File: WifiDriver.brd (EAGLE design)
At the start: 107.6 x 50.8 mm, 8 parts, among them U1 ESP32-DEVKITC-32U, U2 ESP32-DEVKITC-32U, U3 DS18B20

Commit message: Adding files
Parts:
- removed JP2, JP4, JP5: (no value), pinhead:1X05
- added R2, R3, R4, R5: 0, adafruit:R0805
- added U$1: GPS_MOD, brandon_parts:GPS_NEO_6M
- moved R1 40.1 mm to (40.3, 8.59), turned to 90 degrees
- moved U3 28.3 mm to (63.0, 3.70)
- moved U2 21.7 mm to (21.6, 45.1)
- moved U1 20.6 mm to (51.9, 45.0)
- moved JP1 13.3 mm to (70.6, 55.2)
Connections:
- new net ESP_A_RX: R3.1, U1.11
- new net ESP_A_TX: R2.1, U1.12
- new net ESP_B_RX: R4.2, U2.11
- new net ESP_B_TX: R5.2, U2.12
- new net N$2: R3.2, R5.1
- new net N$3: U1.7, U2.15
- net 5V: now also R1.2, U$1.VCC; no longer JP2.5, JP4.3, JP5.3
- net DQ: now also R1.1, U1.26, U3.2; no longer R1.2
- net ESP32_1_RX: no longer JP4.4
- net ESP32_1_TX: no longer JP4.5
- net ESP32_2_RX: no longer JP5.4
- net ESP32_2_TX: no longer JP5.5
- net GND: now also U$1.GND; no longer JP2.4, JP4.1, JP5.1
- net GPS_RX: now also U$1.RXD; no longer JP2.2
- net GPS_TX: now also U$1.TXD; no longer JP2.3
- net N$1: now also R2.2, R4.1; no longer R1.1, U3.2
- net PPS: now also U$1.PPS; no longer JP2.1
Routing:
- net N$1: track 0.00 -> 2.79 mm
- net N$2: track 0.00 -> 2.68 mm
- net CLK: track 2.55 -> 0.00 mm
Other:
- board size 107.6 x 50.8 mm -> 99 x 70.8 mm

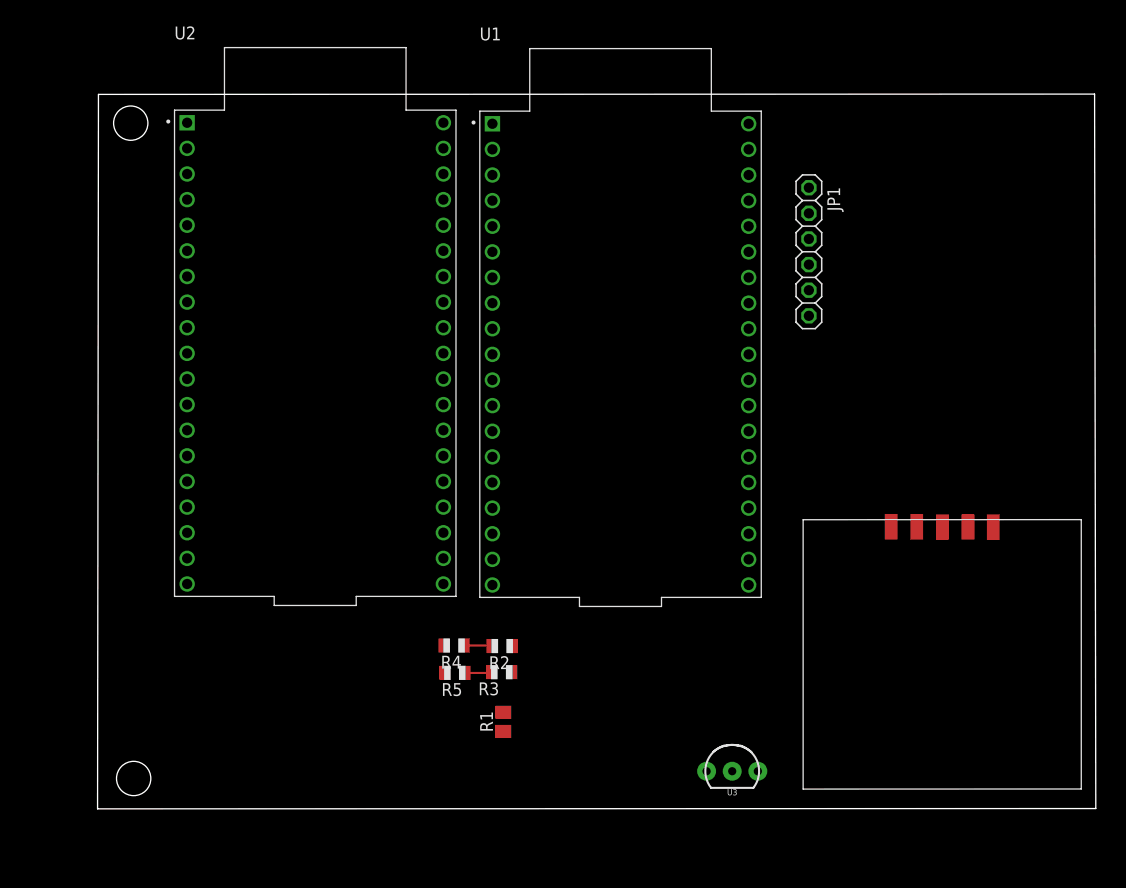
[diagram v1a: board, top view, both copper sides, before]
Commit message: Updated with wardriver_v3 pinout from original author
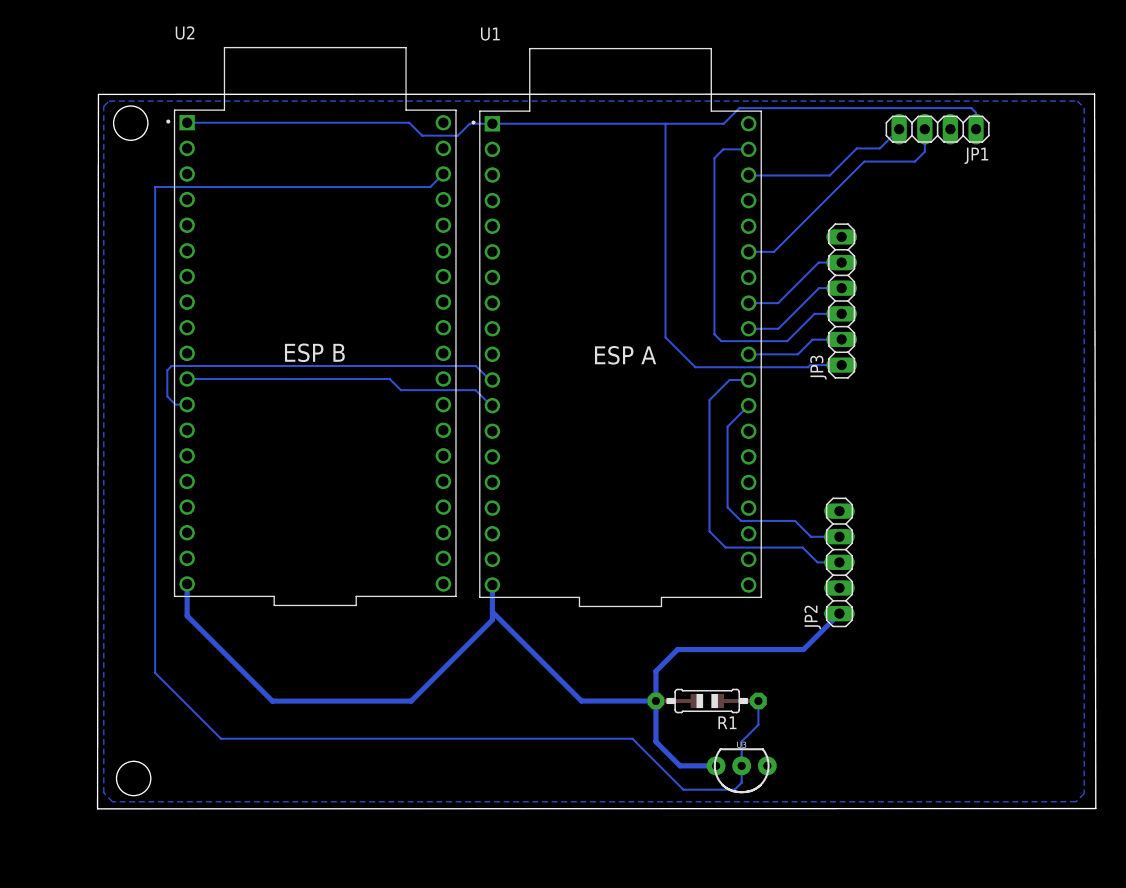
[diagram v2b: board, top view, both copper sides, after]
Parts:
- removed R2, R3, R4, R5: 0, adafruit:R0805
- removed U$1: GPS_MOD, brandon_parts:GPS_NEO_6M
- added JP2: (no value), pinhead:1X05
- added JP3: (no value), pinhead:1X06
- JP1: device adafruit:1X06 -> pinhead:1X04
- R1: value (none) -> 4.7k; device adafruit:M0805 -> adafruit:0805-THM
- moved R1 20.3 mm to (60.5, 10.7), turned to 180 degrees
- moved JP1 17.6 mm to (83.3, 67.3), turned to 180 degrees
- moved U3 1.08 mm to (63.9, 4.23), turned to 180 degrees
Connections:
- removed net ESP32_1_RX: U1.34
- removed net ESP32_1_TX: U1.35
- removed net ESP32_2_RX: U2.34
- removed net ESP32_2_TX: U2.35
- removed net ESP_B_RX: R4.2, U2.11
- removed net ESP_B_TX: R5.2, U2.12
- removed net N$1: R2.2, R4.1
- removed net N$2: R3.2, R5.1
- removed net N$3: U1.7, U2.15
- new net SCL: JP1.4, U1.36
- new net SDA: JP1.3, U1.33
- net 3V3: now also JP3.1
- net 5V: now also JP2.1; no longer U$1.VCC
- net CLK: now also JP3.4; no longer JP1.4
- net CS: now also JP3.2; no longer JP1.2
- net DQ: now also U2.36; no longer U1.26
- net ESP_A_RX: now also U2.12; no longer R3.1
- net ESP_A_TX: now also U2.11; no longer R2.1
- net GND: now also JP1.2, JP2.2, JP3.6; no longer JP1.6, U$1.GND
- net GPS_RX: now also JP2.3, U1.28; no longer U$1.RXD
- net GPS_TX: now also JP2.4, U1.27; no longer U$1.TXD
- net MISO: now also JP3.5; no longer JP1.5
- net MOSI: now also JP3.3; no longer JP1.3
- net PPS: now also JP2.5; no longer U$1.PPS
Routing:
- net DQ: track 0.00 -> 149.3 mm
- net 3V3: track 0.00 -> 121.6 mm
- net 5V: track 0.00 -> 98.5 mm
- net ESP_A_RX: track 0.00 -> 37.9 mm
- net MOSI: track 0.00 -> 35.2 mm
- net GPS_RX: track 0.00 -> 31.9 mm
- net ESP_A_TX: track 0.00 -> 31.5 mm
- net SDA: track 0.00 -> 23.8 mm
- net GPS_TX: track 0.00 -> 23.3 mm
- net SCL: track 0.00 -> 16.8 mm
- net CLK: track 0.00 -> 10.9 mm
- net MISO: track 0.00 -> 10.9 mm
- net CS: track 0.00 -> 9.83 mm
- net N$1: track 2.79 -> 0.00 mm
- net N$2: track 2.68 -> 0.00 mm
- added copper zone on layer 16, net GND
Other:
- board text added: "ESP A"
- board text added: "ESP B"
